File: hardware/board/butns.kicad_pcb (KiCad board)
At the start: 2 copper layers, 99 x 99 mm, 265 parts, among them J1 Conn_01x08, SW1 SW_Push, SW10 SW_Push, SW11 SW_Push, SW12 SW_Push, SW13 SW_Push, SW14 SW_Push, SW15 SW_Push, SW16 SW_Push, SW17 SW_Push, SW18 SW_Push, SW19 SW_Push, SW2 SW_Push, SW20 SW_Push, SW21 SW_Push, SW22 SW_Push, SW23 SW_Push, SW24 SW_Push, SW25 SW_Push, SW26 SW_Push, SW27 SW_Push, SW28 SW_Push, SW29 SW_Push, SW3 SW_Push, SW30 SW_Push, SW31 SW_Push, SW32 SW_Push, SW33 SW_Push, SW34 SW_Push, SW35 SW_Push, SW36 SW_Push, SW37 SW_Push, SW38 SW_Push, SW39 SW_Push, SW4 SW_Push, SW40 SW_Push, SW41 SW_Push, SW42 SW_Push, SW43 SW_Push, SW44 SW_Push, SW45 SW_Push, SW46 SW_Push, SW47 SW_Push, SW48 SW_Push, SW49 SW_Push, SW5 SW_Push, SW50 SW_Push, SW51 SW_Push, SW52 SW_Push, SW53 SW_Push, SW54 SW_Push, SW55 SW_Push, SW56 SW_Push, SW57 SW_Push, SW58 SW_Push, SW59 SW_Push, SW6 SW_Push, SW60 SW_Push, SW61 SW_Push, SW62 SW_Push, SW63 SW_Push, SW64 SW_Push, SW7 SW_Push, SW8 SW_Push, SW9 SW_Push, U1 Pico, U2 74LVC1G17

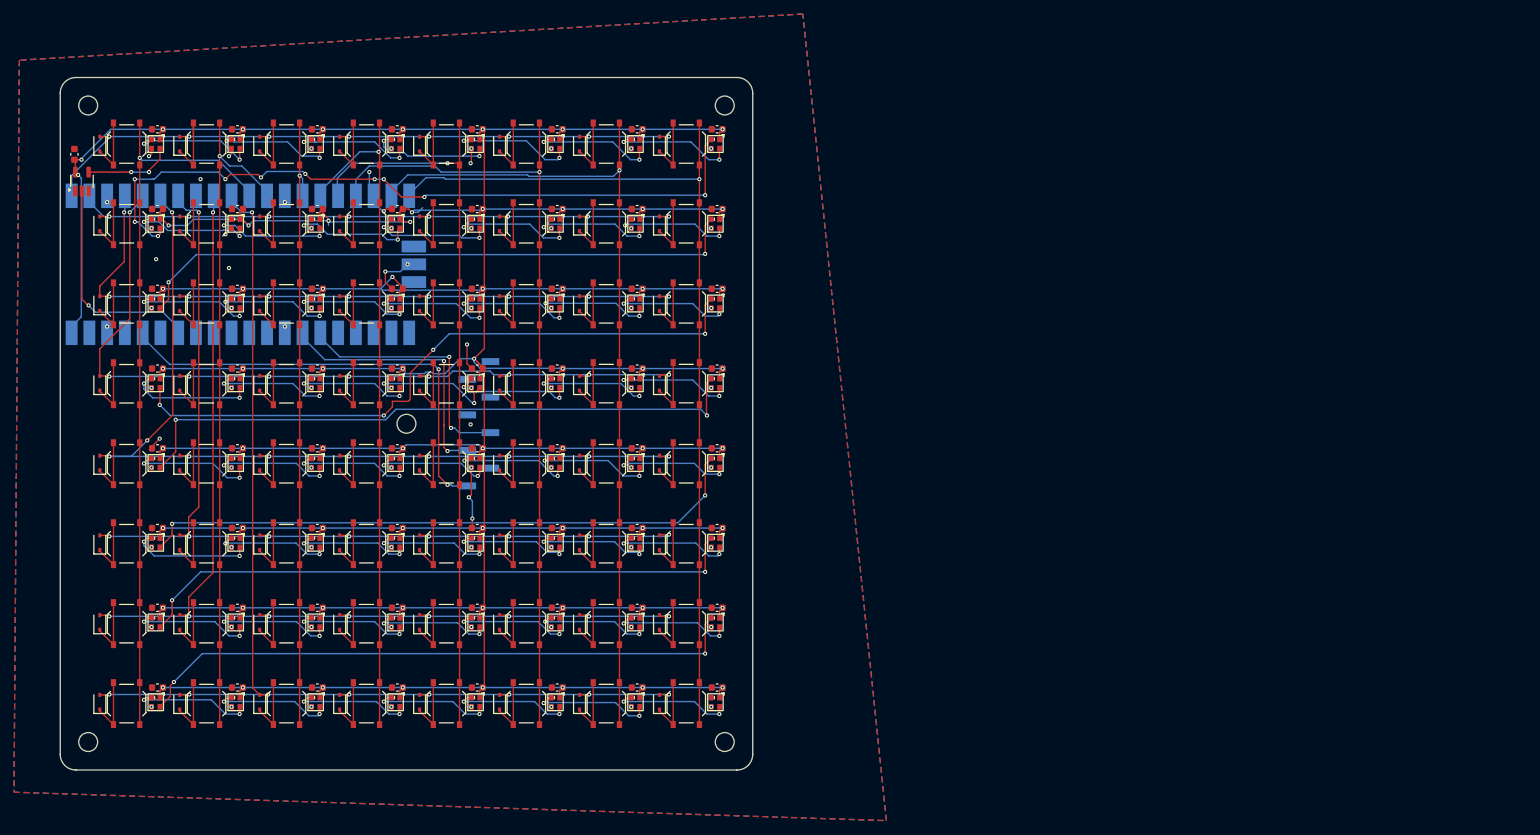
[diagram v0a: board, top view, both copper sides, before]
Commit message: Convert to 16x8 grid (8 rows x 16 columns)
Hardware
- PCB extended to 190.44 x 99 mm with eight additional columns:
  128 switches, 128 diodes, 128 SK6812-EC20, 129 capacitors
- New column nets SW_COL_8..15 on GPIO16-22 and GPIO26, former
  SW_COL_8 (GPIO15) is now SW_COL_16
- LED chain runs row by row over 16 columns
- Tilt header J1 and I2C nets removed, GPIO27 left free
- Second inner mounting hole H6
- Schematic: new sheet butns-frontend2 with the 64 added cells,
  frontend and backend sheets adapted
- Regenerated jlcpcb/ gerbers, BOM and CPL, new butns.step,
  removed stale 8x8 butns.stl and model/butns.wrl

Firmware
- 16 column matrix scan per column with settle time
- LED index row * 16 + col, rotation limited to 0 and 180 degrees
- LED current estimate limited to MAX_LED_CURRENT_MA
- MPU6050 tilt support removed
- Fix led/level/row and led/level/col offset handling

Case
- case.scad and buttons.scad extended to 16 columns, second standoff
- Explicit apply_to argument for roundedcube calls

Co-Authored-By: Claude Opus 5.5 <noreply@anthropic.com>
Claude-Session: https://claude.ai/code/session_0195H63MEXeeVZ7CNyHAeb6N
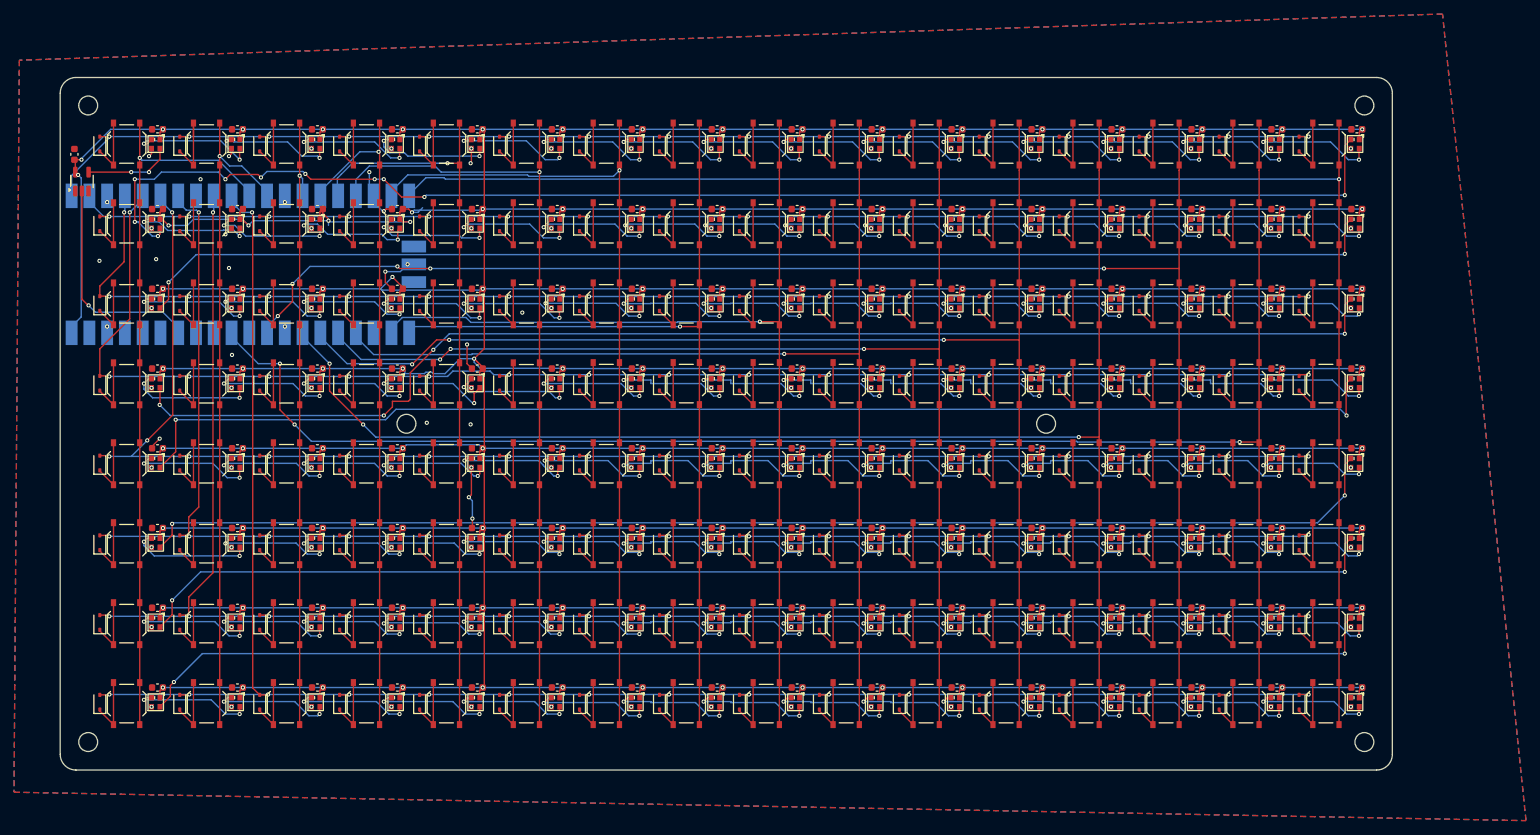
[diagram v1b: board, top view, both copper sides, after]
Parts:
- removed J1: Conn_01x08, Connector_PinHeader_2.54mm:PinHeader_1x08_P2.54mm_Vertical_SMD_Pin1Left
- added C100: 100nF, Capacitor_SMD:C_0603_1608Metric, F.Cu at (249.4, 94.6)
- added C101: 100nF, Capacitor_SMD:C_0603_1608Metric, F.Cu at (260.8, 94.6)
- added C102: 100nF, Capacitor_SMD:C_0603_1608Metric, F.Cu at (272.2, 94.6)
- added C103: 100nF, Capacitor_SMD:C_0603_1608Metric, F.Cu at (283.7, 94.6)
- added C104: 100nF, Capacitor_SMD:C_0603_1608Metric, F.Cu at (295.1, 94.6)
- added C105: 100nF, Capacitor_SMD:C_0603_1608Metric, F.Cu at (306.5, 94.6)
- added C106: 100nF, Capacitor_SMD:C_0603_1608Metric, F.Cu at (226.5, 106.0)
- added C107: 100nF, Capacitor_SMD:C_0603_1608Metric, F.Cu at (237.9, 106.0)
- added C108: 100nF, Capacitor_SMD:C_0603_1608Metric, F.Cu at (249.4, 106.0)
- added C109: 100nF, Capacitor_SMD:C_0603_1608Metric, F.Cu at (260.8, 106.0)
- added C110: 100nF, Capacitor_SMD:C_0603_1608Metric, F.Cu at (272.2, 106.0)
- added C111: 100nF, Capacitor_SMD:C_0603_1608Metric, F.Cu at (283.7, 106.0)
- added C112: 100nF, Capacitor_SMD:C_0603_1608Metric, F.Cu at (295.1, 106.0)
- added C113: 100nF, Capacitor_SMD:C_0603_1608Metric, F.Cu at (306.5, 106.0)
- added C114: 100nF, Capacitor_SMD:C_0603_1608Metric, F.Cu at (226.5, 117.4)
- added C115: 100nF, Capacitor_SMD:C_0603_1608Metric, F.Cu at (237.9, 117.4)
- added C116: 100nF, Capacitor_SMD:C_0603_1608Metric, F.Cu at (249.4, 117.4)
- added C117: 100nF, Capacitor_SMD:C_0603_1608Metric, F.Cu at (260.8, 117.4)
- added C118: 100nF, Capacitor_SMD:C_0603_1608Metric, F.Cu at (272.2, 117.4)
- added C119: 100nF, Capacitor_SMD:C_0603_1608Metric, F.Cu at (283.7, 117.4)
- added C120: 100nF, Capacitor_SMD:C_0603_1608Metric, F.Cu at (295.1, 117.4)
- added C121: 100nF, Capacitor_SMD:C_0603_1608Metric, F.Cu at (306.5, 117.4)
- added C122: 100nF, Capacitor_SMD:C_0603_1608Metric, F.Cu at (226.5, 128.8)
- added C123: 100nF, Capacitor_SMD:C_0603_1608Metric, F.Cu at (237.9, 128.8)
- added C124: 100nF, Capacitor_SMD:C_0603_1608Metric, F.Cu at (249.4, 128.8)
- added C125: 100nF, Capacitor_SMD:C_0603_1608Metric, F.Cu at (260.8, 128.8)
- added C126: 100nF, Capacitor_SMD:C_0603_1608Metric, F.Cu at (272.2, 128.8)
- added C127: 100nF, Capacitor_SMD:C_0603_1608Metric, F.Cu at (283.7, 128.8)
- added C128: 100nF, Capacitor_SMD:C_0603_1608Metric, F.Cu at (295.1, 128.8)
- added C129: 100nF, Capacitor_SMD:C_0603_1608Metric, F.Cu at (306.5, 128.8)
- added C66: 100nF, Capacitor_SMD:C_0603_1608Metric, F.Cu at (226.5, 49.0)
- added C67: 100nF, Capacitor_SMD:C_0603_1608Metric, F.Cu at (237.9, 49.0)
- added C68: 100nF, Capacitor_SMD:C_0603_1608Metric, F.Cu at (249.4, 49.0)
- added C69: 100nF, Capacitor_SMD:C_0603_1608Metric, F.Cu at (260.8, 49.0)
- added C70: 100nF, Capacitor_SMD:C_0603_1608Metric, F.Cu at (272.2, 49.0)
- added C71: 100nF, Capacitor_SMD:C_0603_1608Metric, F.Cu at (283.7, 49.0)
- added C72: 100nF, Capacitor_SMD:C_0603_1608Metric, F.Cu at (295.1, 49.0)
- added C73: 100nF, Capacitor_SMD:C_0603_1608Metric, F.Cu at (306.5, 49.0)
- added C74: 100nF, Capacitor_SMD:C_0603_1608Metric, F.Cu at (226.5, 60.4)
- added C75: 100nF, Capacitor_SMD:C_0603_1608Metric, F.Cu at (237.9, 60.4)
- added C76: 100nF, Capacitor_SMD:C_0603_1608Metric, F.Cu at (249.4, 60.4)
- added C77: 100nF, Capacitor_SMD:C_0603_1608Metric, F.Cu at (260.8, 60.4)
- added C78: 100nF, Capacitor_SMD:C_0603_1608Metric, F.Cu at (272.2, 60.4)
- added C79: 100nF, Capacitor_SMD:C_0603_1608Metric, F.Cu at (283.7, 60.4)
- added C80: 100nF, Capacitor_SMD:C_0603_1608Metric, F.Cu at (295.1, 60.4)
- added C81: 100nF, Capacitor_SMD:C_0603_1608Metric, F.Cu at (306.5, 60.4)
- added C82: 100nF, Capacitor_SMD:C_0603_1608Metric, F.Cu at (226.5, 71.8)
- added C83: 100nF, Capacitor_SMD:C_0603_1608Metric, F.Cu at (237.9, 71.8)
- added C84: 100nF, Capacitor_SMD:C_0603_1608Metric, F.Cu at (249.4, 71.8)
- added C85: 100nF, Capacitor_SMD:C_0603_1608Metric, F.Cu at (260.8, 71.8)
- added C86: 100nF, Capacitor_SMD:C_0603_1608Metric, F.Cu at (272.2, 71.8)
- added C87: 100nF, Capacitor_SMD:C_0603_1608Metric, F.Cu at (283.7, 71.8)
- added C88: 100nF, Capacitor_SMD:C_0603_1608Metric, F.Cu at (295.1, 71.8)
- added C89: 100nF, Capacitor_SMD:C_0603_1608Metric, F.Cu at (306.5, 71.8)
- added C90: 100nF, Capacitor_SMD:C_0603_1608Metric, F.Cu at (226.5, 83.2)
- added C91: 100nF, Capacitor_SMD:C_0603_1608Metric, F.Cu at (237.9, 83.2)
- added C92: 100nF, Capacitor_SMD:C_0603_1608Metric, F.Cu at (249.4, 83.2)
- added C93: 100nF, Capacitor_SMD:C_0603_1608Metric, F.Cu at (260.8, 83.2)
- added C94: 100nF, Capacitor_SMD:C_0603_1608Metric, F.Cu at (272.2, 83.2)
- added C95: 100nF, Capacitor_SMD:C_0603_1608Metric, F.Cu at (283.7, 83.2)
- added C96: 100nF, Capacitor_SMD:C_0603_1608Metric, F.Cu at (295.1, 83.2)
- added C97: 100nF, Capacitor_SMD:C_0603_1608Metric, F.Cu at (306.5, 83.2)
- added C98: 100nF, Capacitor_SMD:C_0603_1608Metric, F.Cu at (226.5, 94.6)
- added C99: 100nF, Capacitor_SMD:C_0603_1608Metric, F.Cu at (237.9, 94.6)
- added D129: 1N4148WS, Diode_SMD:D_SOD-323, F.Cu at (218.3, 51.1)
- added D130: 1N4148WS, Diode_SMD:D_SOD-323, F.Cu at (229.7, 51.1)
- added D131: 1N4148WS, Diode_SMD:D_SOD-323, F.Cu at (241.1, 51.1)
- added D132: 1N4148WS, Diode_SMD:D_SOD-323, F.Cu at (252.6, 51.1)
- added D133: 1N4148WS, Diode_SMD:D_SOD-323, F.Cu at (264.0, 51.1)
- added D134: 1N4148WS, Diode_SMD:D_SOD-323, F.Cu at (275.4, 51.1)
- added D135: 1N4148WS, Diode_SMD:D_SOD-323, F.Cu at (286.8, 51.1)
- added D136: 1N4148WS, Diode_SMD:D_SOD-323, F.Cu at (298.3, 51.1)
- added D137: 1N4148WS, Diode_SMD:D_SOD-323, F.Cu at (218.3, 62.5)
- added D138: 1N4148WS, Diode_SMD:D_SOD-323, F.Cu at (229.7, 62.5)
- added D139: 1N4148WS, Diode_SMD:D_SOD-323, F.Cu at (241.1, 62.5)
- added D140: 1N4148WS, Diode_SMD:D_SOD-323, F.Cu at (252.6, 62.5)
- added D141: 1N4148WS, Diode_SMD:D_SOD-323, F.Cu at (264.0, 62.5)
- added D142: 1N4148WS, Diode_SMD:D_SOD-323, F.Cu at (275.4, 62.5)
- added D143: 1N4148WS, Diode_SMD:D_SOD-323, F.Cu at (286.8, 62.5)
- added D144: 1N4148WS, Diode_SMD:D_SOD-323, F.Cu at (298.3, 62.5)
- added D145: 1N4148WS, Diode_SMD:D_SOD-323, F.Cu at (218.3, 73.9)
- added D146: 1N4148WS, Diode_SMD:D_SOD-323, F.Cu at (229.7, 73.9)
- added D147: 1N4148WS, Diode_SMD:D_SOD-323, F.Cu at (241.1, 73.9)
- added D148: 1N4148WS, Diode_SMD:D_SOD-323, F.Cu at (252.6, 73.9)
- added D149: 1N4148WS, Diode_SMD:D_SOD-323, F.Cu at (264.0, 73.9)
- added D150: 1N4148WS, Diode_SMD:D_SOD-323, F.Cu at (275.4, 73.9)
- added D151: 1N4148WS, Diode_SMD:D_SOD-323, F.Cu at (286.8, 73.9)
- added D152: 1N4148WS, Diode_SMD:D_SOD-323, F.Cu at (298.3, 73.9)
- added D153: 1N4148WS, Diode_SMD:D_SOD-323, F.Cu at (218.3, 85.3)
- added D154: 1N4148WS, Diode_SMD:D_SOD-323, F.Cu at (229.7, 85.3)
- added D155: 1N4148WS, Diode_SMD:D_SOD-323, F.Cu at (241.1, 85.3)
- added D156: 1N4148WS, Diode_SMD:D_SOD-323, F.Cu at (252.6, 85.3)
- added D157: 1N4148WS, Diode_SMD:D_SOD-323, F.Cu at (264.0, 85.3)
- added D158: 1N4148WS, Diode_SMD:D_SOD-323, F.Cu at (275.4, 85.3)
- added D159: 1N4148WS, Diode_SMD:D_SOD-323, F.Cu at (286.8, 85.3)
- added D160: 1N4148WS, Diode_SMD:D_SOD-323, F.Cu at (298.3, 85.3)
- added D161: 1N4148WS, Diode_SMD:D_SOD-323, F.Cu at (218.3, 96.7)
- added D162: 1N4148WS, Diode_SMD:D_SOD-323, F.Cu at (229.7, 96.7)
- added D163: 1N4148WS, Diode_SMD:D_SOD-323, F.Cu at (241.1, 96.7)
- added D164: 1N4148WS, Diode_SMD:D_SOD-323, F.Cu at (252.6, 96.7)
- added D165: 1N4148WS, Diode_SMD:D_SOD-323, F.Cu at (264.0, 96.7)
- added D166: 1N4148WS, Diode_SMD:D_SOD-323, F.Cu at (275.4, 96.7)
- added D167: 1N4148WS, Diode_SMD:D_SOD-323, F.Cu at (286.8, 96.7)
- added D168: 1N4148WS, Diode_SMD:D_SOD-323, F.Cu at (298.3, 96.7)
- added D169: 1N4148WS, Diode_SMD:D_SOD-323, F.Cu at (218.3, 108.1)
- added D170: 1N4148WS, Diode_SMD:D_SOD-323, F.Cu at (229.7, 108.1)
- added D171: 1N4148WS, Diode_SMD:D_SOD-323, F.Cu at (241.1, 108.1)
- added D172: 1N4148WS, Diode_SMD:D_SOD-323, F.Cu at (252.6, 108.1)
- added D173: 1N4148WS, Diode_SMD:D_SOD-323, F.Cu at (264.0, 108.1)
- added D174: 1N4148WS, Diode_SMD:D_SOD-323, F.Cu at (275.4, 108.1)
- added D175: 1N4148WS, Diode_SMD:D_SOD-323, F.Cu at (286.8, 108.1)
- added D176: 1N4148WS, Diode_SMD:D_SOD-323, F.Cu at (298.3, 108.1)
- added D177: 1N4148WS, Diode_SMD:D_SOD-323, F.Cu at (218.3, 119.5)
- added D178: 1N4148WS, Diode_SMD:D_SOD-323, F.Cu at (229.7, 119.5)
- added D179: 1N4148WS, Diode_SMD:D_SOD-323, F.Cu at (241.1, 119.5)
- added D180: 1N4148WS, Diode_SMD:D_SOD-323, F.Cu at (252.6, 119.5)
- added D181: 1N4148WS, Diode_SMD:D_SOD-323, F.Cu at (264.0, 119.5)
- added D182: 1N4148WS, Diode_SMD:D_SOD-323, F.Cu at (275.4, 119.5)
- added D183: 1N4148WS, Diode_SMD:D_SOD-323, F.Cu at (286.8, 119.5)
- added D184: 1N4148WS, Diode_SMD:D_SOD-323, F.Cu at (298.3, 119.5)
- added D185: 1N4148WS, Diode_SMD:D_SOD-323, F.Cu at (218.3, 130.9)
- added D186: 1N4148WS, Diode_SMD:D_SOD-323, F.Cu at (229.7, 130.9)
- added D187: 1N4148WS, Diode_SMD:D_SOD-323, F.Cu at (241.1, 130.9)
- added D188: 1N4148WS, Diode_SMD:D_SOD-323, F.Cu at (252.6, 130.9)
- added D189: 1N4148WS, Diode_SMD:D_SOD-323, F.Cu at (264.0, 130.9)
- added D190: 1N4148WS, Diode_SMD:D_SOD-323, F.Cu at (275.4, 130.9)
- added D191: 1N4148WS, Diode_SMD:D_SOD-323, F.Cu at (286.8, 130.9)
- added D192: 1N4148WS, Diode_SMD:D_SOD-323, F.Cu at (298.3, 130.9)
- added D193: SK6812-EC20, SK6812-EC20:SK6812-EC20, F.Cu at (226.3, 51.1)
- added D194: SK6812-EC20, SK6812-EC20:SK6812-EC20, F.Cu at (237.7, 51.1)
- added D195: SK6812-EC20, SK6812-EC20:SK6812-EC20, F.Cu at (249.1, 51.1)
- added D196: SK6812-EC20, SK6812-EC20:SK6812-EC20, F.Cu at (260.6, 51.1)
- added D197: SK6812-EC20, SK6812-EC20:SK6812-EC20, F.Cu at (272.0, 51.1)
- added D198: SK6812-EC20, SK6812-EC20:SK6812-EC20, F.Cu at (283.4, 51.1)
- added D199: SK6812-EC20, SK6812-EC20:SK6812-EC20, F.Cu at (294.8, 51.1)
- added D200: SK6812-EC20, SK6812-EC20:SK6812-EC20, F.Cu at (306.3, 51.1)
- added D201: SK6812-EC20, SK6812-EC20:SK6812-EC20, F.Cu at (226.3, 62.5)
- added D202: SK6812-EC20, SK6812-EC20:SK6812-EC20, F.Cu at (237.7, 62.5)
- added D203: SK6812-EC20, SK6812-EC20:SK6812-EC20, F.Cu at (249.1, 62.5)
- added D204: SK6812-EC20, SK6812-EC20:SK6812-EC20, F.Cu at (260.6, 62.5)
- added D205: SK6812-EC20, SK6812-EC20:SK6812-EC20, F.Cu at (272.0, 62.5)
- added D206: SK6812-EC20, SK6812-EC20:SK6812-EC20, F.Cu at (283.4, 62.5)
- added D207: SK6812-EC20, SK6812-EC20:SK6812-EC20, F.Cu at (294.8, 62.5)
- added D208: SK6812-EC20, SK6812-EC20:SK6812-EC20, F.Cu at (306.3, 62.5)
- added D209: SK6812-EC20, SK6812-EC20:SK6812-EC20, F.Cu at (226.3, 73.9)
- added D210: SK6812-EC20, SK6812-EC20:SK6812-EC20, F.Cu at (237.7, 73.9)
- added D211: SK6812-EC20, SK6812-EC20:SK6812-EC20, F.Cu at (249.1, 73.9)
- added D212: SK6812-EC20, SK6812-EC20:SK6812-EC20, F.Cu at (260.6, 73.9)
- added D213: SK6812-EC20, SK6812-EC20:SK6812-EC20, F.Cu at (272.0, 73.9)
- added D214: SK6812-EC20, SK6812-EC20:SK6812-EC20, F.Cu at (283.4, 73.9)
- added D215: SK6812-EC20, SK6812-EC20:SK6812-EC20, F.Cu at (294.8, 73.9)
- added D216: SK6812-EC20, SK6812-EC20:SK6812-EC20, F.Cu at (306.3, 73.9)
- added D217: SK6812-EC20, SK6812-EC20:SK6812-EC20, F.Cu at (226.3, 85.3)
- added D218: SK6812-EC20, SK6812-EC20:SK6812-EC20, F.Cu at (237.7, 85.3)
- added D219: SK6812-EC20, SK6812-EC20:SK6812-EC20, F.Cu at (249.1, 85.3)
- added D220: SK6812-EC20, SK6812-EC20:SK6812-EC20, F.Cu at (260.6, 85.3)
- added D221: SK6812-EC20, SK6812-EC20:SK6812-EC20, F.Cu at (272.0, 85.3)
- added D222: SK6812-EC20, SK6812-EC20:SK6812-EC20, F.Cu at (283.4, 85.3)
- added D223: SK6812-EC20, SK6812-EC20:SK6812-EC20, F.Cu at (294.8, 85.3)
- added D224: SK6812-EC20, SK6812-EC20:SK6812-EC20, F.Cu at (306.3, 85.3)
- added D225: SK6812-EC20, SK6812-EC20:SK6812-EC20, F.Cu at (226.3, 96.7)
- added D226: SK6812-EC20, SK6812-EC20:SK6812-EC20, F.Cu at (237.7, 96.7)
- added D227: SK6812-EC20, SK6812-EC20:SK6812-EC20, F.Cu at (249.1, 96.7)
- added D228: SK6812-EC20, SK6812-EC20:SK6812-EC20, F.Cu at (260.6, 96.7)
- added D229: SK6812-EC20, SK6812-EC20:SK6812-EC20, F.Cu at (272.0, 96.7)
- added D230: SK6812-EC20, SK6812-EC20:SK6812-EC20, F.Cu at (283.4, 96.7)
- added D231: SK6812-EC20, SK6812-EC20:SK6812-EC20, F.Cu at (294.8, 96.7)
- added D232: SK6812-EC20, SK6812-EC20:SK6812-EC20, F.Cu at (306.3, 96.7)
- added D233: SK6812-EC20, SK6812-EC20:SK6812-EC20, F.Cu at (226.3, 108.1)
- added D234: SK6812-EC20, SK6812-EC20:SK6812-EC20, F.Cu at (237.7, 108.1)
- added D235: SK6812-EC20, SK6812-EC20:SK6812-EC20, F.Cu at (249.1, 108.1)
- added D236: SK6812-EC20, SK6812-EC20:SK6812-EC20, F.Cu at (260.6, 108.1)
- added D237: SK6812-EC20, SK6812-EC20:SK6812-EC20, F.Cu at (272.0, 108.1)
- added D238: SK6812-EC20, SK6812-EC20:SK6812-EC20, F.Cu at (283.4, 108.1)
- added D239: SK6812-EC20, SK6812-EC20:SK6812-EC20, F.Cu at (294.8, 108.1)
- added D240: SK6812-EC20, SK6812-EC20:SK6812-EC20, F.Cu at (306.3, 108.1)
- added D241: SK6812-EC20, SK6812-EC20:SK6812-EC20, F.Cu at (226.3, 119.5)
- added D242: SK6812-EC20, SK6812-EC20:SK6812-EC20, F.Cu at (237.7, 119.5)
- added D243: SK6812-EC20, SK6812-EC20:SK6812-EC20, F.Cu at (249.1, 119.5)
- added D244: SK6812-EC20, SK6812-EC20:SK6812-EC20, F.Cu at (260.6, 119.5)
- added D245: SK6812-EC20, SK6812-EC20:SK6812-EC20, F.Cu at (272.0, 119.5)
- added D246: SK6812-EC20, SK6812-EC20:SK6812-EC20, F.Cu at (283.4, 119.5)
- added D247: SK6812-EC20, SK6812-EC20:SK6812-EC20, F.Cu at (294.8, 119.5)
- added D248: SK6812-EC20, SK6812-EC20:SK6812-EC20, F.Cu at (306.3, 119.5)
- added D249: SK6812-EC20, SK6812-EC20:SK6812-EC20, F.Cu at (226.3, 130.9)
- added D250: SK6812-EC20, SK6812-EC20:SK6812-EC20, F.Cu at (237.7, 130.9)
- added D251: SK6812-EC20, SK6812-EC20:SK6812-EC20, F.Cu at (249.1, 130.9)
- added D252: SK6812-EC20, SK6812-EC20:SK6812-EC20, F.Cu at (260.6, 130.9)
- added D253: SK6812-EC20, SK6812-EC20:SK6812-EC20, F.Cu at (272.0, 130.9)
- added D254: SK6812-EC20, SK6812-EC20:SK6812-EC20, F.Cu at (283.4, 130.9)
- added D255: SK6812-EC20, SK6812-EC20:SK6812-EC20, F.Cu at (294.8, 130.9)
- added D256: SK6812-EC20, SK6812-EC20:SK6812-EC20, F.Cu at (306.3, 130.9)
- added H6: MountingHole, MountingHole:MountingHole_2.7mm_M2.5, F.Cu at (273.5, 91.1)
- added SW100: SW_Push, switch:SW_Push_1P1T_XKB_TS-1187A, F.Cu at (256.4, 96.8)
- added SW101: SW_Push, switch:SW_Push_1P1T_XKB_TS-1187A, F.Cu at (267.8, 96.8)
- added SW102: SW_Push, switch:SW_Push_1P1T_XKB_TS-1187A, F.Cu at (279.2, 96.8)
- added SW103: SW_Push, switch:SW_Push_1P1T_XKB_TS-1187A, F.Cu at (290.7, 96.8)
- added SW104: SW_Push, switch:SW_Push_1P1T_XKB_TS-1187A, F.Cu at (302.1, 96.8)
- added SW105: SW_Push, switch:SW_Push_1P1T_XKB_TS-1187A, F.Cu at (222.1, 108.2)
- added SW106: SW_Push, switch:SW_Push_1P1T_XKB_TS-1187A, F.Cu at (233.5, 108.2)
- added SW107: SW_Push, switch:SW_Push_1P1T_XKB_TS-1187A, F.Cu at (245.0, 108.2)
- added SW108: SW_Push, switch:SW_Push_1P1T_XKB_TS-1187A, F.Cu at (256.4, 108.2)
- added SW109: SW_Push, switch:SW_Push_1P1T_XKB_TS-1187A, F.Cu at (267.8, 108.2)
- added SW110: SW_Push, switch:SW_Push_1P1T_XKB_TS-1187A, F.Cu at (279.2, 108.2)
- added SW111: SW_Push, switch:SW_Push_1P1T_XKB_TS-1187A, F.Cu at (290.7, 108.2)
- added SW112: SW_Push, switch:SW_Push_1P1T_XKB_TS-1187A, F.Cu at (302.1, 108.2)
- added SW113: SW_Push, switch:SW_Push_1P1T_XKB_TS-1187A, F.Cu at (222.1, 119.7)
- added SW114: SW_Push, switch:SW_Push_1P1T_XKB_TS-1187A, F.Cu at (233.5, 119.7)
- added SW115: SW_Push, switch:SW_Push_1P1T_XKB_TS-1187A, F.Cu at (245.0, 119.7)
- added SW116: SW_Push, switch:SW_Push_1P1T_XKB_TS-1187A, F.Cu at (256.4, 119.7)
- added SW117: SW_Push, switch:SW_Push_1P1T_XKB_TS-1187A, F.Cu at (267.8, 119.7)
- added SW118: SW_Push, switch:SW_Push_1P1T_XKB_TS-1187A, F.Cu at (279.2, 119.7)
- added SW119: SW_Push, switch:SW_Push_1P1T_XKB_TS-1187A, F.Cu at (290.7, 119.7)
- added SW120: SW_Push, switch:SW_Push_1P1T_XKB_TS-1187A, F.Cu at (302.1, 119.7)
- added SW121: SW_Push, switch:SW_Push_1P1T_XKB_TS-1187A, F.Cu at (222.1, 131.1)
- added SW122: SW_Push, switch:SW_Push_1P1T_XKB_TS-1187A, F.Cu at (233.5, 131.1)
- added SW123: SW_Push, switch:SW_Push_1P1T_XKB_TS-1187A, F.Cu at (245.0, 131.1)
- added SW124: SW_Push, switch:SW_Push_1P1T_XKB_TS-1187A, F.Cu at (256.4, 131.1)
- added SW125: SW_Push, switch:SW_Push_1P1T_XKB_TS-1187A, F.Cu at (267.8, 131.1)
- added SW126: SW_Push, switch:SW_Push_1P1T_XKB_TS-1187A, F.Cu at (279.2, 131.1)
- added SW127: SW_Push, switch:SW_Push_1P1T_XKB_TS-1187A, F.Cu at (290.7, 131.1)
- added SW128: SW_Push, switch:SW_Push_1P1T_XKB_TS-1187A, F.Cu at (302.1, 131.1)
- added SW65: SW_Push, switch:SW_Push_1P1T_XKB_TS-1187A, F.Cu at (222.1, 51.1)
- added SW66: SW_Push, switch:SW_Push_1P1T_XKB_TS-1187A, F.Cu at (233.5, 51.1)
- added SW67: SW_Push, switch:SW_Push_1P1T_XKB_TS-1187A, F.Cu at (245.0, 51.1)
- added SW68: SW_Push, switch:SW_Push_1P1T_XKB_TS-1187A, F.Cu at (256.4, 51.1)
- added SW69: SW_Push, switch:SW_Push_1P1T_XKB_TS-1187A, F.Cu at (267.8, 51.1)
- added SW70: SW_Push, switch:SW_Push_1P1T_XKB_TS-1187A, F.Cu at (279.2, 51.1)
- added SW71: SW_Push, switch:SW_Push_1P1T_XKB_TS-1187A, F.Cu at (290.7, 51.1)
- added SW72: SW_Push, switch:SW_Push_1P1T_XKB_TS-1187A, F.Cu at (302.1, 51.1)
- added SW73: SW_Push, switch:SW_Push_1P1T_XKB_TS-1187A, F.Cu at (222.1, 62.5)
- added SW74: SW_Push, switch:SW_Push_1P1T_XKB_TS-1187A, F.Cu at (233.5, 62.5)
- added SW75: SW_Push, switch:SW_Push_1P1T_XKB_TS-1187A, F.Cu at (245.0, 62.5)
- added SW76: SW_Push, switch:SW_Push_1P1T_XKB_TS-1187A, F.Cu at (256.4, 62.5)
- added SW77: SW_Push, switch:SW_Push_1P1T_XKB_TS-1187A, F.Cu at (267.8, 62.5)
- added SW78: SW_Push, switch:SW_Push_1P1T_XKB_TS-1187A, F.Cu at (279.2, 62.5)
- added SW79: SW_Push, switch:SW_Push_1P1T_XKB_TS-1187A, F.Cu at (290.7, 62.5)
- added SW80: SW_Push, switch:SW_Push_1P1T_XKB_TS-1187A, F.Cu at (302.1, 62.5)
- added SW81: SW_Push, switch:SW_Push_1P1T_XKB_TS-1187A, F.Cu at (222.1, 74.0)
- added SW82: SW_Push, switch:SW_Push_1P1T_XKB_TS-1187A, F.Cu at (233.5, 74.0)
- added SW83: SW_Push, switch:SW_Push_1P1T_XKB_TS-1187A, F.Cu at (245.0, 74.0)
- added SW84: SW_Push, switch:SW_Push_1P1T_XKB_TS-1187A, F.Cu at (256.4, 74.0)
- added SW85: SW_Push, switch:SW_Push_1P1T_XKB_TS-1187A, F.Cu at (267.8, 74.0)
- added SW86: SW_Push, switch:SW_Push_1P1T_XKB_TS-1187A, F.Cu at (279.2, 74.0)
- added SW87: SW_Push, switch:SW_Push_1P1T_XKB_TS-1187A, F.Cu at (290.7, 74.0)
- added SW88: SW_Push, switch:SW_Push_1P1T_XKB_TS-1187A, F.Cu at (302.1, 74.0)
- added SW89: SW_Push, switch:SW_Push_1P1T_XKB_TS-1187A, F.Cu at (222.1, 85.3)
- added SW90: SW_Push, switch:SW_Push_1P1T_XKB_TS-1187A, F.Cu at (233.5, 85.3)
- added SW91: SW_Push, switch:SW_Push_1P1T_XKB_TS-1187A, F.Cu at (245.0, 85.3)
- added SW92: SW_Push, switch:SW_Push_1P1T_XKB_TS-1187A, F.Cu at (256.4, 85.3)
- added SW93: SW_Push, switch:SW_Push_1P1T_XKB_TS-1187A, F.Cu at (267.8, 85.3)
- added SW94: SW_Push, switch:SW_Push_1P1T_XKB_TS-1187A, F.Cu at (279.2, 85.3)
- added SW95: SW_Push, switch:SW_Push_1P1T_XKB_TS-1187A, F.Cu at (290.7, 85.3)
- added SW96: SW_Push, switch:SW_Push_1P1T_XKB_TS-1187A, F.Cu at (302.1, 85.3)
- added SW97: SW_Push, switch:SW_Push_1P1T_XKB_TS-1187A, F.Cu at (222.1, 96.8)
- added SW98: SW_Push, switch:SW_Push_1P1T_XKB_TS-1187A, F.Cu at (233.5, 96.8)
- added SW99: SW_Push, switch:SW_Push_1P1T_XKB_TS-1187A, F.Cu at (245.0, 96.8)
- moved SW16 91.4 mm to (313.5, 62.5)
- moved SW24 91.4 mm to (313.5, 74.0)
- moved SW32 91.4 mm to (313.5, 85.3)
- moved SW40 91.4 mm to (313.5, 96.8)
- moved SW48 91.4 mm to (313.5, 108.2)
- moved SW56 91.4 mm to (313.5, 119.7)
- moved SW64 91.4 mm to (313.5, 131.1)
- moved SW8 91.4 mm to (313.5, 51.1)
- moved C16 91.4 mm to (317.9, 60.4)
- moved C24 91.4 mm to (317.9, 71.8)
- moved C32 91.4 mm to (317.9, 83.2)
- moved C40 91.4 mm to (317.9, 94.6)
- moved C48 91.4 mm to (317.9, 106.0)
- moved C56 91.4 mm to (317.9, 117.4)
- moved C64 91.4 mm to (317.9, 128.8)
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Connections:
- D103 pad 2: Net-(D103-DOUT) -> LED_R5_A
- D104 pad 4: Net-(D103-DOUT) -> LED_R5_B
- D111 pad 2: Net-(D111-DOUT) -> LED_R6_A
- D112 pad 4: Net-(D111-DOUT) -> LED_R6_B
- D119 pad 2: Net-(D119-DOUT) -> LED_R7_A
- D120 pad 4: Net-(D119-DOUT) -> LED_R7_B
- D127 pad 2: Net-(D127-DOUT) -> LED_R8_A
- D128 pad 4: Net-(D127-DOUT) -> LED_R8_B
- D71 pad 2: Net-(D71-DOUT) -> LED_R1_A
- D72 pad 4: Net-(D71-DOUT) -> LED_R1_B
- D79 pad 2: Net-(D79-DOUT) -> LED_R2_A
- D80 pad 4: Net-(D79-DOUT) -> LED_R2_B
- D87 pad 2: Net-(D87-DOUT) -> LED_R3_A
- D88 pad 4: Net-(D87-DOUT) -> LED_R3_B
- D95 pad 2: Net-(D95-DOUT) -> LED_R4_A
- D96 pad 4: Net-(D95-DOUT) -> LED_R4_B
- SW16 pad 2: SW_COL_8 -> SW_COL_16
- SW24 pad 2: SW_COL_8 -> SW_COL_16
- SW32 pad 2: SW_COL_8 -> SW_COL_16
- SW40 pad 2: SW_COL_8 -> SW_COL_16
- SW48 pad 2: SW_COL_8 -> SW_COL_16
- SW56 pad 2: SW_COL_8 -> SW_COL_16
- SW64 pad 2: SW_COL_8 -> SW_COL_16
- SW8 pad 2: SW_COL_8 -> SW_COL_16
- U1 pad 20: SW_COL_8 -> SW_COL_16
- U1 pad 21: unconnected-(U1-GPIO16-Pad21) -> SW_COL_8
- U1 pad 22: unconnected-(U1-GPIO17-Pad22) -> SW_COL_9
- U1 pad 24: unconnected-(U1-GPIO18-Pad24) -> SW_COL_10
- U1 pad 25: unconnected-(U1-GPIO19-Pad25) -> SW_COL_11
- U1 pad 26: I2C0_SDA -> SW_COL_12
- U1 pad 27: I2C0_SCL -> SW_COL_13
- U1 pad 29: unconnected-(U1-GPIO22-Pad29) -> SW_COL_14
- U1 pad 31: unconnected-(U1-GPIO26_ADC0-Pad31) -> SW_COL_15
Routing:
- net +5V: track 886.6 -> 1722.2 mm, vias 67 -> 131
- net SW_COL_15: track 0.00 -> 244.5 mm, vias 0 -> 3
- net SW_COL_14: track 0.00 -> 221.5 mm, vias 0 -> 5
- net SW_COL_16: track 0.00 -> 221.1 mm, vias 0 -> 1
- net SW_COL_13: track 0.00 -> 209.6 mm, vias 0 -> 3
- net SW_COL_12: track 0.00 -> 190.5 mm, vias 0 -> 3
- net SW_COL_11: track 0.00 -> 175.4 mm, vias 0 -> 3
- net SW_COL_10: track 0.00 -> 160.5 mm, vias 0 -> 1
- net SW_COL_9: track 0.00 -> 142.4 mm, vias 0 -> 1
- net SW_ROW_4: track 119.4 -> 222.3 mm, vias 9 -> 17
- net SW_ROW_7: track 152.2 -> 255.1 mm, vias 9 -> 17
- net SW_ROW_6: track 141.9 -> 244.7 mm, vias 9 -> 17
- net SW_ROW_8: track 164.3 -> 266.8 mm, vias 9 -> 17
- net SW_ROW_3: track 106.0 -> 208.5 mm, vias 9 -> 17
- net SW_ROW_1: track 102.5 -> 204.9 mm, vias 8 -> 16
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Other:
- board size 99 x 99 mm -> 190.4 x 99 mm
- board text removed: "GND"
- board text removed: "SCL"
- board text removed: "SDA"
- board text removed: "VCC"
